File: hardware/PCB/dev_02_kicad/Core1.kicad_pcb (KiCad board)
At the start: 2 copper layers, 50.3 x 44.5 mm, 27 parts, among them P1 USB_OTG, P3 CONN_01X04, P4 Mic_IN, P5 MCP3201, P7 USB_OTG, P8 CONN_01X04, SW1 SW_PUSH, U1 ESP-07v2, U2 LM1117-3.3, U3 FT232RL

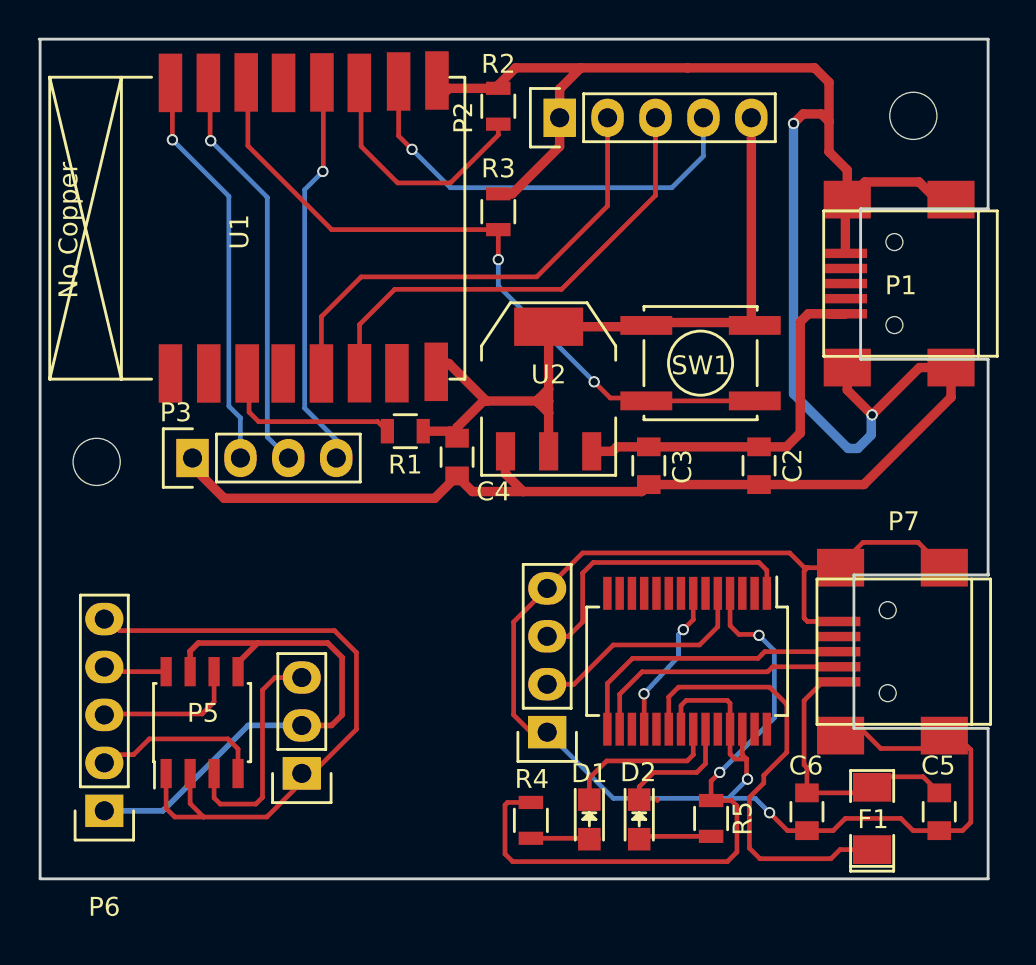
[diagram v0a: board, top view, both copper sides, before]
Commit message: UDPServer
Hela UDP Server projecktet
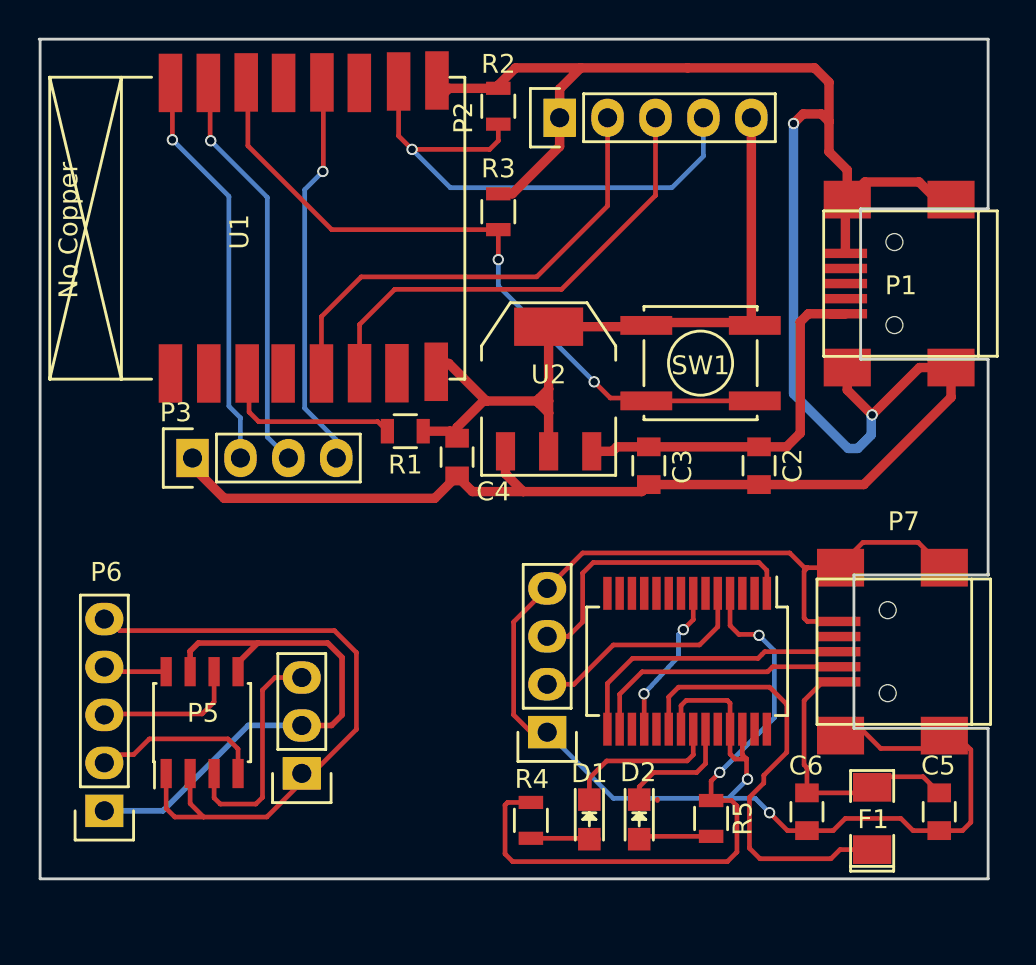
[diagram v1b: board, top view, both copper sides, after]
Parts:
- removed ? (x2): , Mounting_Holes:MountingHole_2.5mm
- P2: value (none) -> Pinhead SMD Connector
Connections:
- R2 pad 1: Net-(R2-Pad1) -> SS
- U1 pad 11: Net-(R2-Pad1) -> (no net)
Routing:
- net Net-(R2-Pad1): track 12.1 -> 0.00 mm
- net SS: track 22.2 -> 27.8 mm
